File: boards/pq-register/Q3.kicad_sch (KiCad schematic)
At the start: 51 parts, among them Q101 T1-N652, Q63 T1-N652, Q83 T1-N652, Q84 T1-N652, Q85 T1-N652, Q86 T1-N652, Q87 T1-N652, Q88 T1-N652

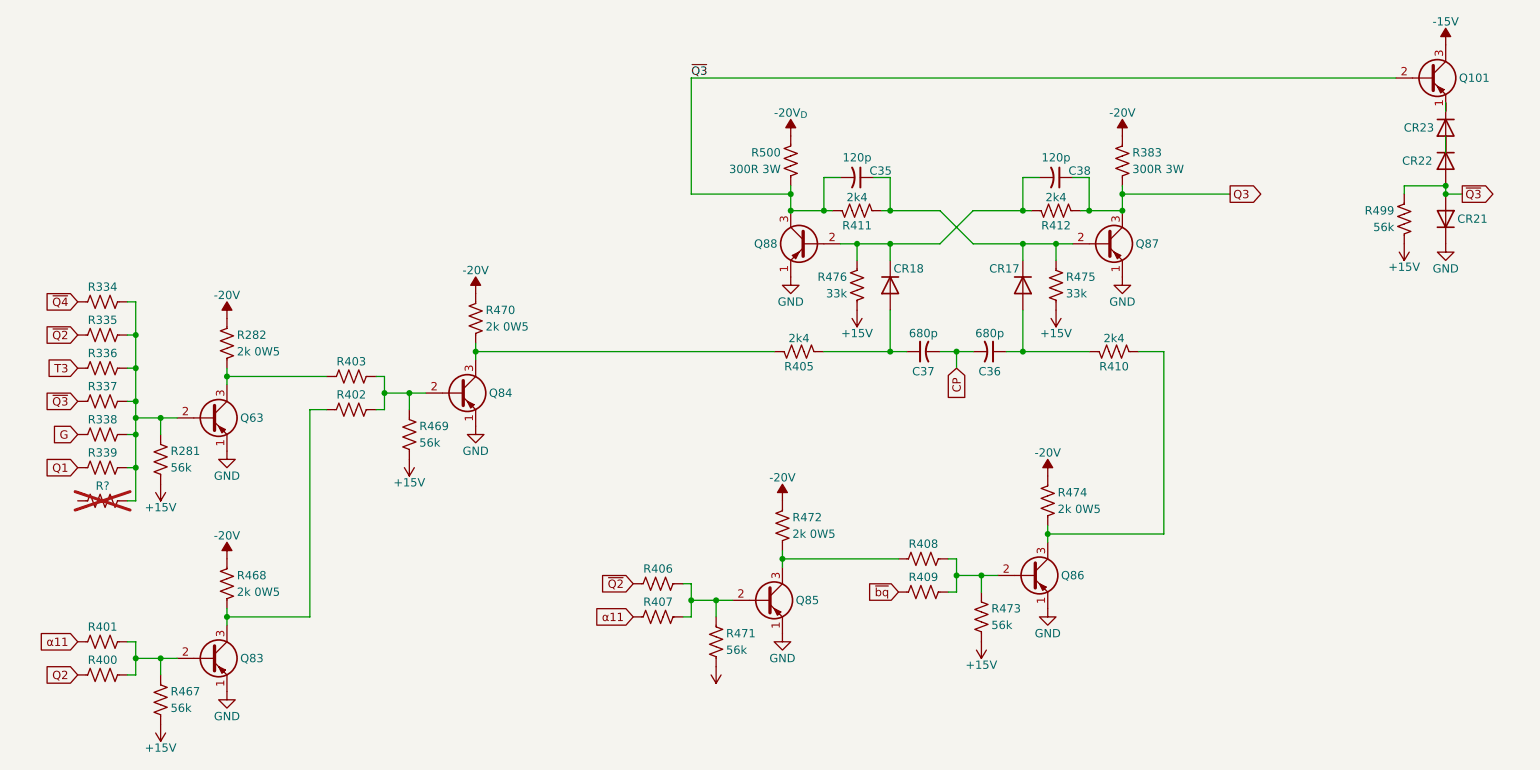
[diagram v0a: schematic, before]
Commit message: Run ERC and clean up P & Q Register board.
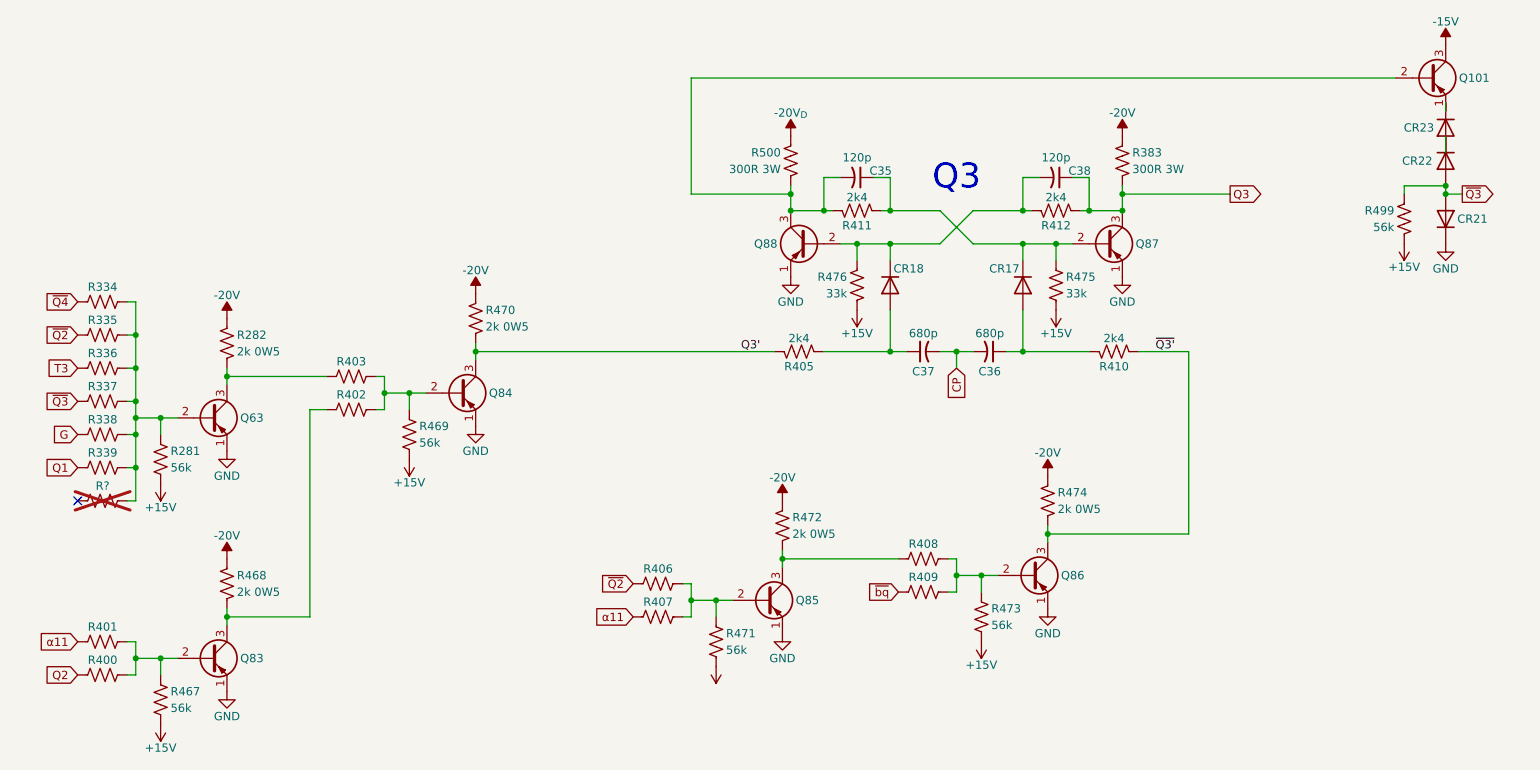
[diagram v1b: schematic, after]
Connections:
- net ~{Q3}: no longer C35.2, Q101.2 (B), Q88.3 (C), R411.1, R500.2
- net Q3': now reaches Q84.3 (C), R405.1, R470.2
- net ~{Q3'}: now reaches Q86.3 (C), R410.2, R474.2
- new net: C35.2, Q101.2 (B), Q88.3 (C), R411.1, R500.2
- no-connect marks 0 -> 1
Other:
- note added: "Q3"

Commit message: Add copyright information.
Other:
- company: (none) -> © 1962 General Precision; redrawn by Sam Hanes
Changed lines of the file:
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@@
 	(title_block
 		(title "LGP-21 P & Q Register Board")
+		(date "2026-06-15")
+		(rev "ESD 1060")
+		(company "© 1962 General Precision; redrawn by Sam Hanes")
+		(comment 1 "https://github.com/Elemecca/lgp21-docs")
 	)
 	(text "Q3"
